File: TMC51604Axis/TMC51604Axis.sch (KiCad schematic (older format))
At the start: 16 parts

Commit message: Sync
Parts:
- removed C? (x2): 2.2u, symbol Device:C_Small
- removed C?: 470n, symbol Device:C_Small
- removed C? (x4): C_Small, symbol Device:C_Small
- removed C?: 22n/100v, symbol Device:C_Small
- removed C?: 100n/16v, symbol Device:C_Small
- removed C?: 100n, symbol Device:C_Small
- removed R?: 2R2, symbol Device:R_Small
- removed R? (x4): 47R, symbol Device:R
- removed U?: TMC5160-TA, eTQFP48_9x9, symbol 2019-09-25_19-26-57:TMC5160-TA
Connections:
- net labels removed: +12V, +3V3, +VMotor, GND
- wire segments 25 -> 0

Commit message: Sync
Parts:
- added Q1: LTC4359IMS8_PBF, digikey-footprints:TSSOP-8_W3mm, symbol dk_PMIC-OR-Controllers-Ideal-Diodes:LTC4359IMS8_PBF
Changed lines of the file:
@@
 F1 "MotorDrv1.sch" 50
 $EndSheet
+$Comp
+L dk_PMIC-OR-Controllers-Ideal-Diodes:LTC4359IMS8_PBF Q1
+U 1 1 5E013102
+P 5050 2650
+F 0 "Q1" H 4850 3200 60  0000 C CNN
+F 1 "LTC4359IMS8_PBF" H 5050 3050 60  0000 C CNN
+F 2 "digikey-footprints:TSSOP-8_W3mm" H 5250 2850 60  0001 L CNN
+F 3 "http://www.analog.com/media/en/technical-documentation/data-sheets/ltc4359.pdf" H 5250 2950 60  0001 L CNN
+F 4 "LTC4359IMS8#PBF-ND" H 5250 3050 60  0001 L CNN "Digi-Key_PN"
+F 5 "LTC4359IMS8#PBF" H 5250 3150 60  0001 L CNN "MPN"
+F 6 "Integrated Circuits (ICs)" H 5250 3250 60  0001 L CNN "Category"
+F 7 "PMIC - OR Controllers, Ideal Diodes" H 5250 3350 60  0001 L CNN "Family"
+F 8 "http://www.analog.com/media/en/technical-documentation/data-sheets/ltc4359.pdf" H 5250 3450 60  0001 L CNN "DK_Datasheet_Link"
+F 9 "/product-detail/en/linear-technology-analog-devices/LTC4359IMS8-PBF/LTC4359IMS8-PBF-ND/3306829" H 5250 3550 60  0001 L CNN "DK_Detail_Page"
+F 10 "IC OR CTRLR N+1 8MSOP" H 5250 3650 60  0001 L CNN "Description"
+F 11 "Linear Technology/Analog Devices" H 5250 3750 60  0001 L CNN "Manufacturer"
+F 12 "Active" H 5250 3850 60  0001 L CNN "Status"
+	1    5050 2650
+	1    0    0    -1
+$EndComp
 $EndSCHEMATC

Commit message: Layout done! Still untested
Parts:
- removed Q1: LTC4359IMS8_PBF, digikey-footprints:TSSOP-8_W3mm, symbol dk_PMIC-OR-Controllers-Ideal-Diodes:LTC4359IMS8_PBF
- added C1: 330n, peters:C_0805_peter, symbol Device:C_Small
- added C10: 10u, Capacitor_SMD:C_0603_1608Metric, symbol Device:C
- added C11: 1uF, peters:C_0805_peter, symbol Device:C
- added C12: 100p, peters:C_0805_peter, symbol Device:C
- added C13: 220p, peters:C_0805_peter, symbol Device:C
- added C14: 22nF, peters:C_0805_peter, symbol Device:C_Small
- added C2: 10p, peters:C_0805_peter, symbol Device:C_Small
- added C3: 10uF/100v, Capacitor_SMD:CP_Elec_8x6.2, symbol Device:CP
- added C4: 22uF/100v, Capacitor_SMD:CP_Elec_8x6.2, symbol Device:C
- added C5: 47nF, peters:C_0805_peter, symbol Device:C
- added C6: 2.2uF, peters:C_0805_peter, symbol Device:C
- added C7: 47u/25V, Capacitor_THT:CP_Radial_D10.0mm_P5.00mm, symbol Device:CP
- added C9: 100n, Capacitor_SMD:C_0603_1608Metric, symbol Device:C
- added D1: 1N4148W, Diode_SMD:D_SOD-123, symbol Diode:1N4148W
- added D2: 7V, Diode_SMD:D_1206_3216Metric, symbol Device:D_Zener
- added D3: 10V, Diode_SMD:D_1206_3216Metric, symbol Device:D_Zener
- added D4: LED, Diode_SMD:D_0805_2012Metric, symbol Device:LED
- added D5: LT1766, Package_SO:TSSOP-16-1EP_4.4x5mm_P0.65mm, symbol Peters:LT1766
- added D6: D_Schottky, Diode_SMD:D_SOD-123F, symbol Device:D_Schottky
- added F1: Fuse, Fuse:Fuse_2512_6332Metric, symbol Device:Fuse
- added FB2: MPZ2012S601A, Resistor_SMD:R_0805_2012Metric_Pad1.15x1.40mm_HandSolder, symbol Device:Ferrite_Bead
- added H1, H2, H3, H4: MountingHole, MountingHole:MountingHole_3.2mm_M3, symbol Mechanical:MountingHole
- added J1: +48Vin, Connector_Phoenix_MSTB:PhoenixContact_MSTB_2,5_2-GF_1x02_P5.00mm_Horizontal_ThreadedFlange_MountHole, symbol Connector:Conn_01x02_Female
- added J2: Stepper_conn, TerminalBlock_Phoenix:TerminalBlock_Phoenix_PT-1,5-4-3.5-H_1x04_P3.50mm_Horizontal, symbol Connector:Screw_Terminal_01x04
- added L1: 33uH, Inductor_SMD:L_7.3x7.3_H3.5, symbol Device:L
- added Q1: SUD08P06-155L, Package_TO_SOT_SMD:TO-252-2, symbol Transistor_FET:SUD08P06-155L
- added R1: 0R01, Resistor_SMD:R_2512_6332Metric, symbol Device:R
- added R2: 36K5, peters:R_0805_peter, symbol Device:R_Small
- added R3: 100k, peters:R_0805_peter, symbol Device:R
- added R4: 10K, peters:R_0805_peter, symbol Device:R
- added R5: 4K12, peters:R_0805_peter, symbol Device:R_Small
- added R6: 2k2, peters:R_0805_peter, symbol Device:R_Small
- added TP1, TP2, TP4, TP5, TP6, TP7: TestPoint, TestPoint:TestPoint_Pad_1.5x1.5mm, symbol Connector:TestPoint
- added U1: AP2210-3.3V, Package_TO_SOT_SMD:SOT-23-5_HandSoldering, symbol Peters:AP2210-3.3V
- added U2: LM2937, Package_TO_SOT_SMD:SOT-223-3_TabPin2, symbol Peters:LM2937
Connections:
- new net: C13.1, D5.11 (VC), R6.1
- new net: D5.12 (FB), R2.2, R5.1
- new net: C1.2, D5.2 (SW), D6.1 (K), L1.1
- new net: C1.1, D1.1 (K), D5.6 (BOOST)
- new net: D1.2 (A), D2.2 (A)
- new net: C14.1, R6.2
- new net: F1.2, J1.2 (Pin_2)
- new net: C2.2, C5.1, D3.1 (K), Q1.3 (S), R1.1, TP1.1
- new net: C12.1, U1.4 (Bypass)
- new net: D3.2 (A), Q1.1 (G), R3.1
- new net: F1.1, Q1.2 (D)
- new net: C9.1, FB2.1, U2.1 (VIN)
- new net: D4.1 (K), R4.1
- new net +12V: C7.1, D2.1 (K), D5.10 (BIAS), FB2.2, L1.2, R2.1, TP4.1
- new net +3V3: C6.1, TP6.1, U1.5 (VOut)
- new net +48V: C2.1, C3.1, C4.1, D4.2 (A), D5.4 (VIN), R1.2, TP2.1
- new net +5V: C10.1, C11.1, TP5.1, U1.1 (VIN), U1.3 (ENA), U2.3 (VOUT)
- new net GND: C10.2, C11.2, C12.2, C13.2, C14.2, C3.2, C4.2, C5.2, C6.2, C7.2, C9.2, D5.1 (GND), D5.14 (SYNC), D5.16 (GND), D5.17 (GND), D5.8 (GND), D5.9 (GND), D6.2 (A), J1.1 (Pin_1), R3.2, R4.2, R5.2, TP7.1, U1.2 (GND), U2.2 (GND)
- new net MotorDrv1/StepperA: J2.1 (Pin_1)
- new net MotorDrv1/StepperB: J2.2 (Pin_2)
- new net MotorDrv1/StepperC: J2.3 (Pin_3)
- new net MotorDrv1/StepperD: J2.4 (Pin_4)

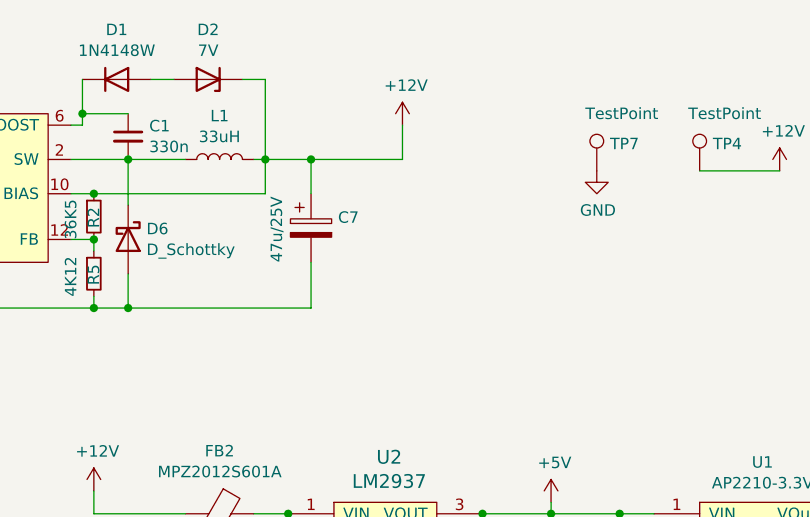
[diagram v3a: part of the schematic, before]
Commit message: Redone input section
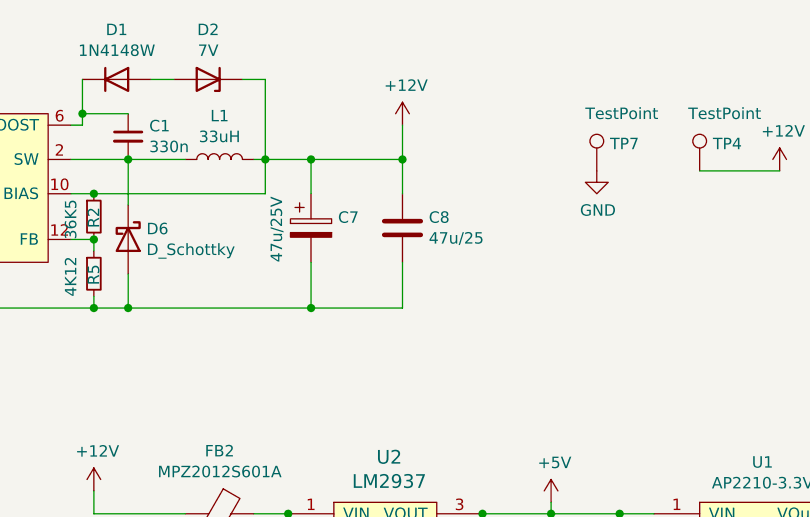
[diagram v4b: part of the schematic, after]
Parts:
- added C8: 47u/25, Capacitor_SMD:C_2010_5025Metric_Pad1.52x2.65mm_HandSolder, symbol Device:C
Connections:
- net +12V: now also C8.1
- net GND: now also C8.2
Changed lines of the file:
@@
 	7200 1200 7600 1200
 $Comp
-L power:+12V #PWR?
+L power:+12V #PWR0103
 U 1 1 5F8D8D2B
 P 9250 1250
-F 0 "#PWR?" H 9250 1100 50  0001 C CNN
+F 0 "#PWR0103" H 9250 1100 50  0001 C CNN
 F 1 "+12V" H 9265 1423 50  0000 C CNN
 F 2 "" H 9250 1250 50  0001 C CNN
@@
 	9250 1250 8900 1250
 $Comp
-L power:+5V #PWR?
+L power:+5V #PWR0104
 U 1 1 5F8DDF9A
 P 9900 1250
-F 0 "#PWR?" H 9900 1100 50  0001 C CNN
+F 0 "#PWR0104" H 9900 1100 50  0001 C CNN
 F 1 "+5V" H 9915 1423 50  0000 C CNN
 F 2 "" H 9900 1250 50  0001 C CNN
@@
 	9650 2750 10150 2750
 $Comp
-L Peters:+3.3V #PWR?
+L Peters:+3.3V #PWR0105
 U 1 1 5F8E2D13
 P 10500 1250
-F 0 "#PWR?" H 10500 1100 50  0001 C CNN
+F 0 "#PWR0105" H 10500 1100 50  0001 C CNN
 F 1 "+3.3V" H 10515 1423 50  0000 C CNN
 F 2 "" H 10500 1250 50  0001 C CNN
@@
 Wire Wire Line
 	10500 1250 10100 1250
+$Comp
+L Device:C C8
+U 1 1 5F8FCFC8
+P 7600 1500
+F 0 "C8" H 7715 1546 50  0000 L CNN
+F 1 "47u/25" H 7715 1455 50  0000 L CNN
+F 2 "Capacitor_SMD:C_2010_5025Metric_Pad1.52x2.65mm_HandSolder" H 7638 1350 50  0001 C CNN
+F 3 "~" H 7600 1500 50  0001 C CNN
+	1    7600 1500
+	1    0    0    -1
+$EndComp
+Wire Wire Line
+	7600 1200 7600 1350
+Wire Wire Line
+	7600 1850 7200 1850
+Wire Wire Line
+	7600 1650 7600 1850
+Connection ~ 7600 1200
+Connection ~ 7200 1850
 $EndSCHEMATC

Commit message: Ver0.1 done
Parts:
- TP1, TP2: footprint TestPoint:TestPoint_Pad_1.5x1.5mm -> TestPoint:TestPoint_Pad_D1.5mm
- TP7: footprint TestPoint:TestPoint_Pad_1.5x1.5mm -> TestPoint:TestPoint_THTPad_1.5x1.5mm_Drill0.7mm
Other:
- moved on the sheet: C5, TP1
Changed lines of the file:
@@
 L Device:C C5
 U 1 1 5ED05A0D
-P 2750 1300
-F 0 "C5" H 2550 1300 50  0000 L CNN
-F 1 "47nF" H 2550 1150 50  0000 L CNN
-F 2 "peters:C_0805_peter" H 2788 1150 50  0001 C CNN
-F 3 "~" H 2750 1300 50  0001 C CNN
-	1    2750 1300
+P 2550 1300
+F 0 "C5" H 2350 1300 50  0000 L CNN
+F 1 "47nF" H 2350 1150 50  0000 L CNN
+F 2 "peters:C_0805_peter" H 2588 1150 50  0001 C CNN
+F 3 "~" H 2550 1300 50  0001 C CNN
+	1    2550 1300
 	1    0    0    -1
 $EndComp
@@
 	1600 1050 1400 1050
 Wire Wire Line
-	2750 1450 2750 1750
-Wire Wire Line
-	2750 1750 1800 1750
+	2550 1450 2550 1750
+Wire Wire Line
+	2550 1750 1800 1750
 Connection ~ 1800 1750
 $Comp
@@
 L Connector:TestPoint TP1
 U 1 1 5ED2B264
-P 2750 950
-F 0 "TP1" H 2808 1068 50  0000 L CNN
-F 1 "TestPoint" H 2650 1200 50  0000 L CNN
-F 2 "TestPoint:TestPoint_Pad_1.5x1.5mm" H 2950 950 50  0001 C CNN
-F 3 "~" H 2950 950 50  0001 C CNN
-	1    2750 950
+P 2550 950
+F 0 "TP1" H 2608 1068 50  0000 L CNN
+F 1 "TestPoint" H 2450 1200 50  0000 L CNN
+F 2 "TestPoint:TestPoint_Pad_D1.5mm" H 2750 950 50  0001 C CNN
+F 3 "~" H 2750 950 50  0001 C CNN
+	1    2550 950
 	1    0    0    -1
 $EndComp
@@
 F 0 "TP2" H 3408 1068 50  0000 L CNN
 F 1 "TestPoint" H 3300 1200 50  0000 L CNN
-F 2 "TestPoint:TestPoint_Pad_1.5x1.5mm" H 3550 950 50  0001 C CNN
+F 2 "TestPoint:TestPoint_Pad_D1.5mm" H 3550 950 50  0001 C CNN
 F 3 "~" H 3550 950 50  0001 C CNN
 	1    3350 950
@@
 $EndComp
 Wire Wire Line
-	2750 950  2750 1050
-Wire Wire Line
-	2750 1050 2800 1050
+	2550 950  2550 1050
+Wire Wire Line
+	2550 1050 2800 1050
 Wire Wire Line
 	3200 1050 3350 1050
@@
 	3550 1150 3550 1050
 Wire Wire Line
-	3550 1750 2750 1750
-Connection ~ 2750 1750
+	3550 1750 2550 1750
+Connection ~ 2550 1750
 $Comp
 L Device:Fuse F1
@@
 $EndComp
 Wire Wire Line
-	2750 1150 2750 1050
-Connection ~ 2750 1050
+	2550 1150 2550 1050
+Connection ~ 2550 1050
 $Comp
 L Device:C_Small C2
@@
 L power:GND #PWR0101
 U 1 1 5ECAFA60
-P 2750 1750
-F 0 "#PWR0101" H 2750 1500 50  0001 C CNN
-F 1 "GND" H 2755 1577 50  0000 C CNN
-F 2 "" H 2750 1750 50  0001 C CNN
-F 3 "" H 2750 1750 50  0001 C CNN
-	1    2750 1750
-	1    0    0    -1
-$EndComp
-Wire Wire Line
-	2100 1050 2750 1050
+P 2550 1750
+F 0 "#PWR0101" H 2550 1500 50  0001 C CNN
+F 1 "GND" H 2555 1577 50  0000 C CNN
+F 2 "" H 2550 1750 50  0001 C CNN
+F 3 "" H 2550 1750 50  0001 C CNN
+	1    2550 1750
+	1    0    0    -1
+$EndComp
+Wire Wire Line
+	2100 1050 2550 1050
 $Comp
 L Connector:TestPoint TP4
@@
 F 0 "TP7" H 8508 1368 50  0000 L CNN
 F 1 "TestPoint" H 8400 1500 50  0000 L CNN
-F 2 "TestPoint:TestPoint_Pad_1.5x1.5mm" H 8650 1250 50  0001 C CNN
+F 2 "TestPoint:TestPoint_THTPad_1.5x1.5mm_Drill0.7mm" H 8650 1250 50  0001 C CNN
 F 3 "~" H 8650 1250 50  0001 C CNN
 	1    8450 1250
